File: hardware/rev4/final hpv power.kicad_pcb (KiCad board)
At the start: 2 copper layers, 38.7 x 68.5 mm, 32 parts, among them J1 Conn_01x12, J2 Conn_01x04_Pin, J3 USB_C_Receptacle_USB2.0_14P, Q1 PNP, SW2 SW_SPST, U1 ESP32-S3-WROOM-1, U2 MCP1825S, U3 HX711

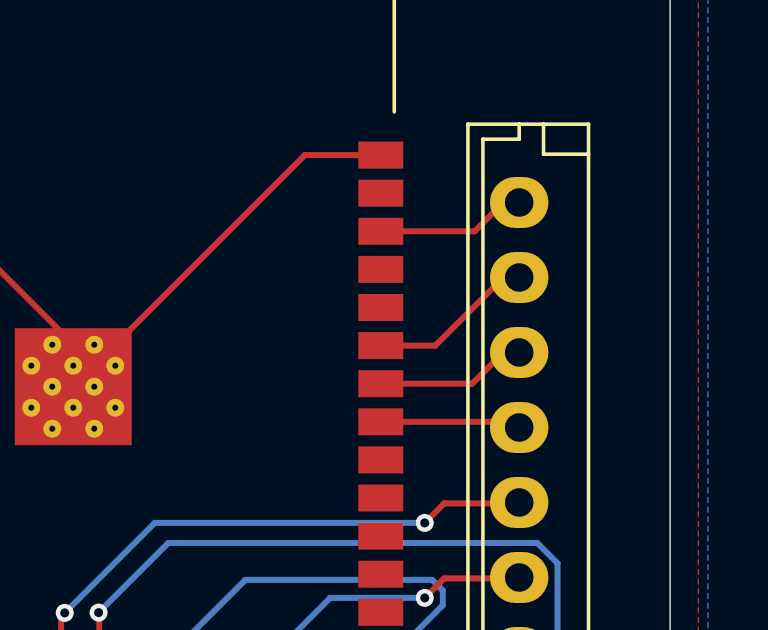
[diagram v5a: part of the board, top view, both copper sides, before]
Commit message: connected TX and RX pins on MCU to header
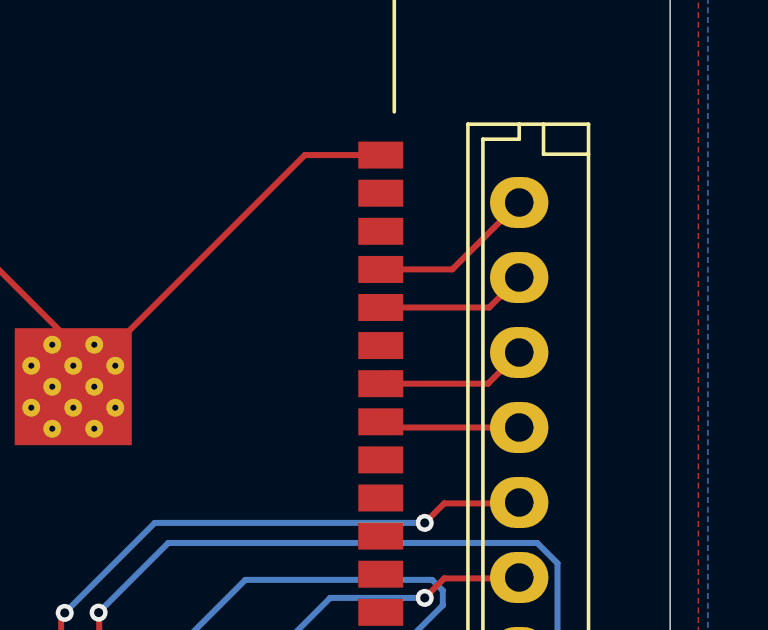
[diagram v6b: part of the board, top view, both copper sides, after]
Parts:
- C1: value 1uF -> 1u
- C10, C11, C2: value 0.1uF -> 0.1u
- C12, C3, C9: value 10uF -> 10u
- J1: value Conn_01x12 -> ~
- J2: value Conn_01x04_Pin -> ~
- J3: value USB_C_Receptacle_USB2.0_14P -> ~
- Q1: value PNP -> ~
- SW2: value SW_SPST -> ~
- U1: value ESP32-S3-WROOM-1 -> ~
- U2: value MCP1825S -> ~
- U3: value HX711 -> ~
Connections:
- J1 pad 10: /GPIO11 -> /GPIO9
- J1 pad 11: /GPIO10 -> /RX
- J1 pad 12: /GPIO9 -> /TX
- J1 pad 9: /GPIO12 -> /GPIO10
- U1 pad 33: /GPIO12 -> /GPIO10
- U1 pad 34: /GPIO11 -> /GPIO9
- U1 pad 35: /GPIO10 -> unconnected-(U1-IO42-Pad35)
- U1 pad 36: unconnected-(U1-RXD0-Pad36) -> /RX
- U1 pad 37: unconnected-(U1-TXD0-Pad37) -> /TX
- U1 pad 38: /GPIO9 -> unconnected-(U1-IO2-Pad38)
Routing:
- net /TX: track 0.00 -> 5.54 mm
- net /RX: track 0.00 -> 5.03 mm
- net /GPIO11: track 4.98 -> 0.00 mm
- net /GPIO12: track 4.15 -> 0.00 mm
- net /GPIO9: track 4.44 -> 5.55 mm

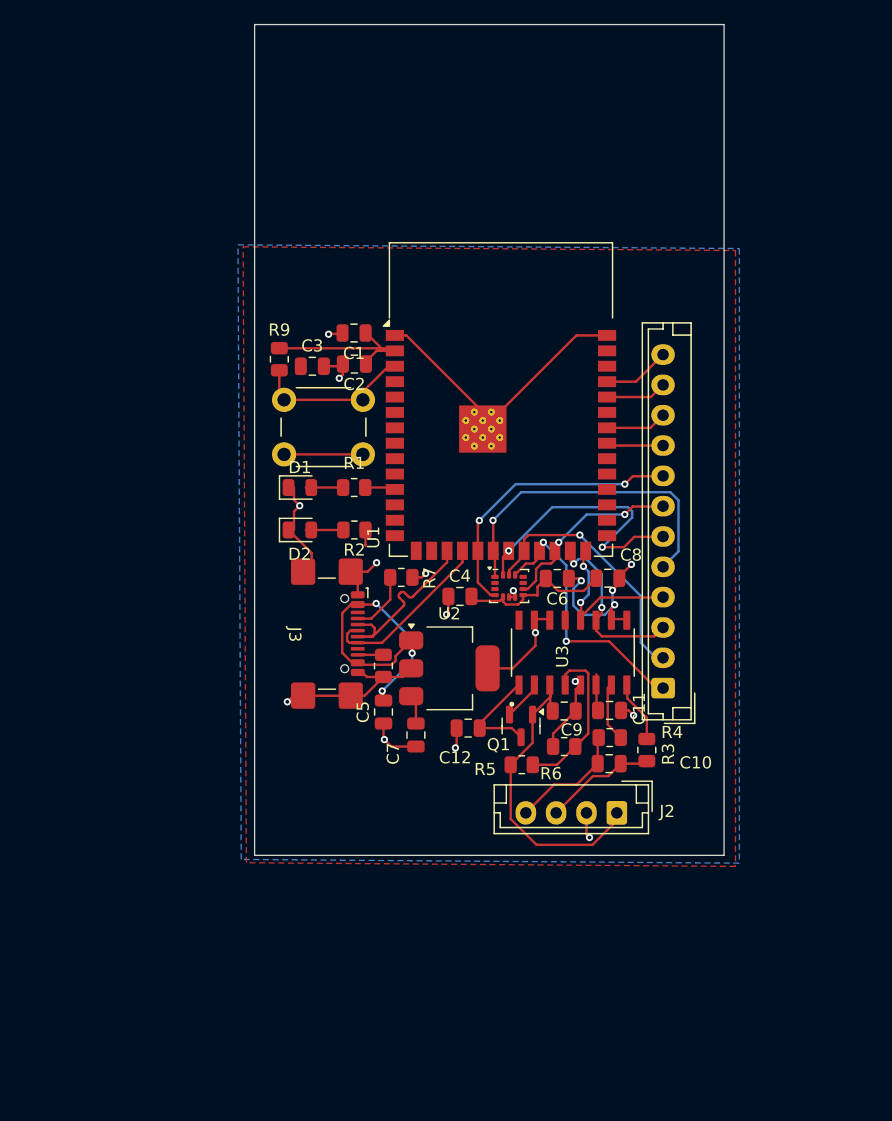
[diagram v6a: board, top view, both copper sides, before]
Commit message: last fixes
moved usb cconnector to edge, added more silkscreen, added tx and rx to breakout header
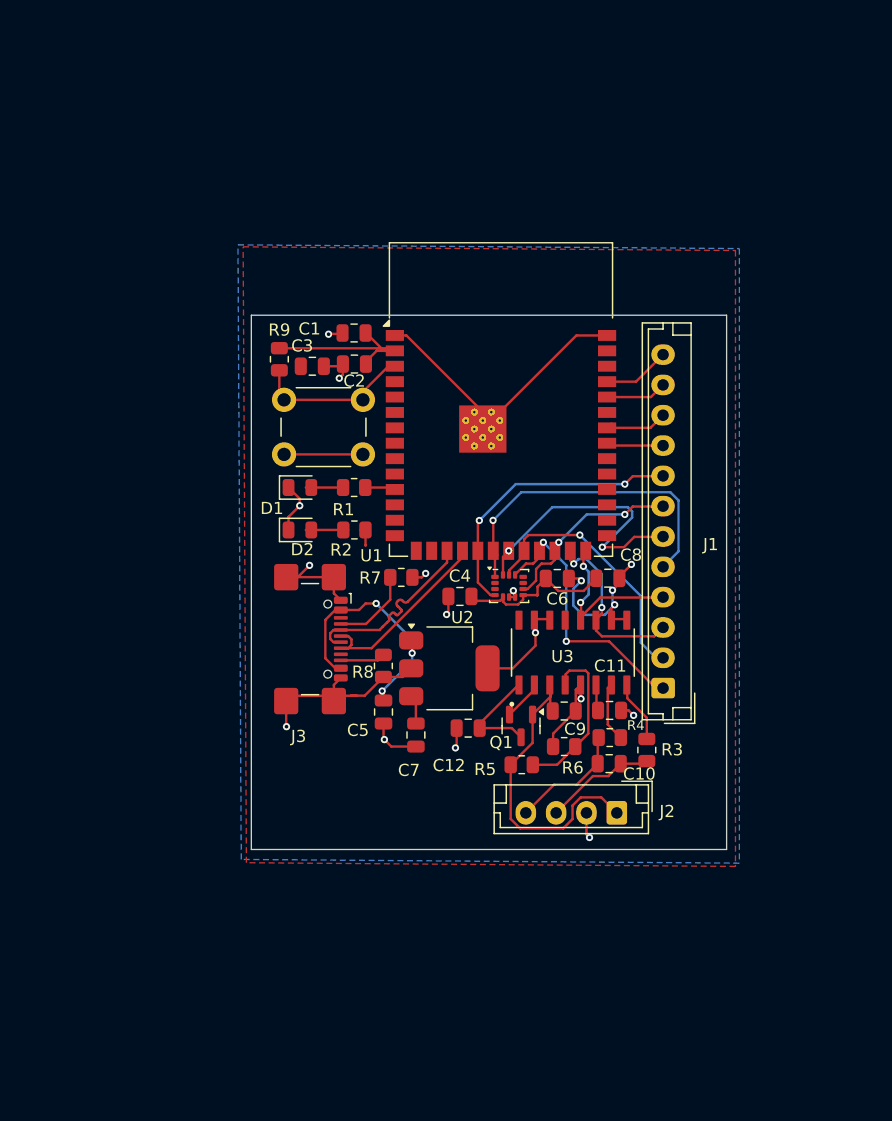
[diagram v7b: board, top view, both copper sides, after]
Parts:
- moved J3 1.47 mm to (122.4, 101.8)
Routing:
- net VBUS: track 24.9 -> 20.9 mm
- net Net-(J3-CC1): track 4.66 -> 6.74 mm
- net GND: track 105.0 -> 107.0 mm
- net /D+: track 14.3 -> 16.1 mm
- net /D-: track 14.2 -> 16.0 mm
- net Net-(J3-CC2): track 2.12 -> 3.70 mm
- net Net-(J2-Pin_1): track 26.2 -> 27.1 mm
- net Net-(U3-VBG): track 3.03 -> 2.24 mm
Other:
- board size 38.7 x 68.5 mm -> 39.2 x 44.1 mm

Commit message: Final fixes
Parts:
- moved R3 2.19 mm to (153.5, 110.9)
- moved R4 2.11 mm to (148.1, 112.0)
- moved C10 2.08 mm to (148.6, 110.0)
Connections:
- C10 pad 1: Net-(J2-Pin_3) -> Net-(U3-INA+)
- C10 pad 2: Net-(J2-Pin_4) -> Net-(U3-INA-)
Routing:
- net Net-(U3-INA+): track 5.21 -> 10.5 mm
- net Net-(U3-INA-): track 5.02 -> 7.35 mm
- net Net-(J2-Pin_4): track 10.1 -> 7.87 mm
- net Net-(J2-Pin_3): track 9.51 -> 11.7 mm
- net Net-(U3-VFB): track 13.5 -> 15.5 mm
